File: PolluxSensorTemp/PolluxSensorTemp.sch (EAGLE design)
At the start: 0 parts

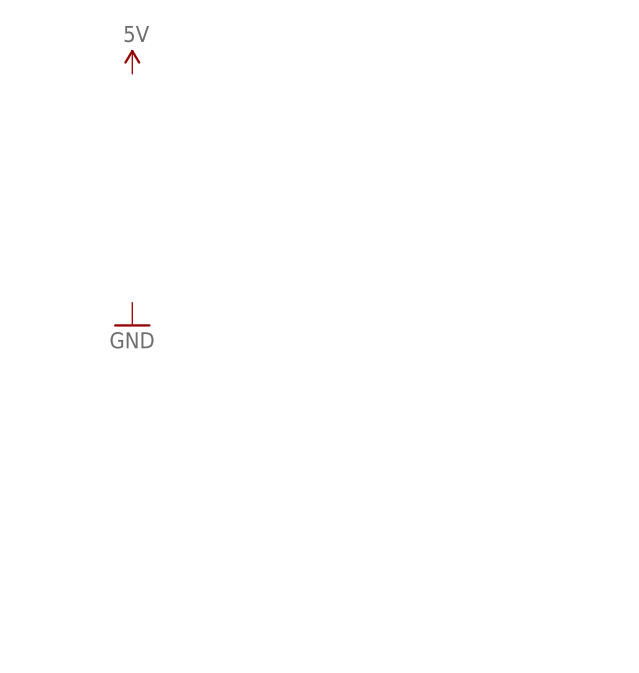
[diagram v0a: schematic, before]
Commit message: add Temp sensor board and schematics
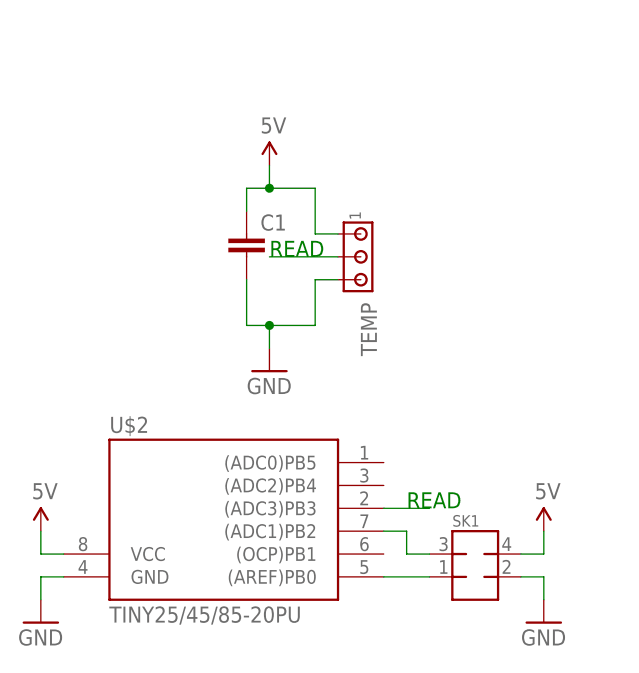
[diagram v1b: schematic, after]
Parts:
- added C1: (no value), SparkFun:CAPPTH1
- added SK1: (no value), jt-con-micromatch:MMATCH-8-PTH
- added TEMP: (no value), con-amp:MTA03-100
- added U$2: TINY25/45/85-20PU, avr-7:TINY25/45/85-20PU
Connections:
- new net 5V: C1.1, SK1.4, TEMP.1, U$2.VCC
- new net GND: C1.2, SK1.2, TEMP.3, U$2.GND
- new net N$1: SK1.3, U$2.(ADC1)PB2
- new net N$2: SK1.1, U$2.(AREF)PB0
- new net READ: TEMP.2, U$2.(ADC3)PB3
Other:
- note added: "READ"
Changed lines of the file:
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@@
 </classes>
 <parts>
+<part name="GND1" library="SparkFun" deviceset="GND" device=""/>
+<part name="SK1" library="jt-con-micromatch" deviceset="MMATCH-8-*" device="PTH"/>
+<part name="U$2" library="avr-7" deviceset="TINY25/45/85" device="-20PU"/>
+<part name="U$3" library="SparkFun" deviceset="5V" device=""/>
+<part name="U$4" library="SparkFun" deviceset="5V" device=""/>
+<part name="GND2" library="SparkFun" deviceset="GND" device=""/>
+<part name="TEMP" library="con-amp" deviceset="MTA03-100" device=""/>
+<part name="C1" library="SparkFun" deviceset="CAP" device="PTH1"/>
 <part name="U$1" library="SparkFun" deviceset="5V" device=""/>
-<part name="GND1" library="SparkFun" deviceset="GND" device=""/>
+<part name="GND3" library="SparkFun" deviceset="GND" device=""/>
 </parts>
 <sheets>
 <sheet>
 <plain>
+<text x="58.42" y="58.42" size="1.778" layer="91">READ</text>
+<text x="73.66" y="30.48" size="1.778" layer="91">READ</text>
 </plain>
 <instances>
-<instance part="U$1" gate="G$1" x="43.18" y="78.74"/>
-<instance part="GND1" gate="1" x="43.18" y="50.8"/>
+<instance part="GND1" gate="1" x="88.9" y="17.78"/>
+<instance part="SK1" gate="G$1" x="81.28" y="22.86"/>
+<instance part="U$2" gate="G$1" x="53.34" y="27.94"/>
+<instance part="U$3" gate="G$1" x="33.02" y="27.94"/>
+<instance part="U$4" gate="G$1" x="88.9" y="27.94"/>
+<instance part="GND2" gate="1" x="33.02" y="17.78"/>
+<instance part="TEMP" gate="G$1" x="68.58" y="58.42" rot="R270"/>
+<instance part="C1" gate="G$1" x="55.88" y="58.42"/>
+<instance part="U$1" gate="G$1" x="58.42" y="68.58"/>
+<instance part="GND3" gate="1" x="58.42" y="45.72"/>
 </instances>
 <busses>
 </busses>
 <nets>
+<net name="N$2" class="0">
+<segment>
+<pinref part="SK1" gate="G$1" pin="1"/>
+<pinref part="U$2" gate="G$1" pin="(AREF)PB0"/>
+<wire x1="76.2" y1="22.86" x2="71.12" y2="22.86" width="0.1524" layer="91"/>
+</segment>
+</net>
+<net name="5V" class="0">
+<segment>
+<pinref part="SK1" gate="G$1" pin="4"/>
+<wire x1="86.36" y1="25.4" x2="88.9" y2="25.4" width="0.1524" layer="91"/>
+<pinref part="U$4" gate="G$1" pin="5V"/>
+<wire x1="88.9" y1="25.4" x2="88.9" y2="27.94" width="0.1524" layer="91"/>
+</segment>
+<segment>
+<pinref part="U$2" gate="G$1" pin="VCC"/>
+<wire x1="35.56" y1="25.4" x2="33.02" y2="25.4" width="0.1524" layer="91"/>
+<pinref part="U$3" gate="G$1" pin="5V"/>
+<wire x1="33.02" y1="25.4" x2="33.02" y2="27.94" width="0.1524" layer="91"/>
+</segment>
+<segment>
+<pinref part="C1" gate="G$1" pin="1"/>
+<wire x1="55.88" y1="63.5" x2="55.88" y2="66.04" width="0.1524" layer="91"/>
+<wire x1="55.88" y1="66.04" x2="58.42" y2="66.04" width="0.1524" layer="91"/>
+<wire x1="58.42" y1="66.04" x2="63.5" y2="66.04" width="0.1524" layer="91"/>
+<wire x1="63.5" y1="66.04" x2="63.5" y2="60.96" width="0.1524" layer="91"/>
+<pinref part="TEMP" gate="G$1" pin="1"/>
+<wire x1="63.5" y1="60.96" x2="66.04" y2="60.96" width="0.1524" layer="91"/>
+<pinref part="U$1" gate="G$1" pin="5V"/>
+<wire x1="58.42" y1="68.58" x2="58.42" y2="66.04" width="0.1524" layer="91"/>
+<junction x="58.42" y="66.04"/>
+</segment>
+</net>
+<net name="GND" class="0">
+<segment>
+<pinref part="U$2" gate="G$1" pin="GND"/>
+<wire x1="35.56" y1="22.86" x2="33.02" y2="22.86" width="0.1524" layer="91"/>
+<pinref part="GND2" gate="1" pin="GND"/>
+<wire x1="33.02" y1="22.86" x2="33.02" y2="20.32" width="0.1524" layer="91"/>
+</segment>
+<segment>
+<pinref part="SK1" gate="G$1" pin="2"/>
+<wire x1="86.36" y1="22.86" x2="88.9" y2="22.86" width="0.1524" layer="91"/>
+<pinref part="GND1" gate="1" pin="GND"/>
+<wire x1="88.9" y1="22.86" x2="88.9" y2="20.32" width="0.1524" layer="91"/>
+</segment>
+<segment>
+<wire x1="58.42" y1="50.8" x2="63.5" y2="50.8" width="0.1524" layer="91"/>
+<wire x1="63.5" y1="50.8" x2="63.5" y2="55.88" width="0.1524" layer="91"/>
+<pinref part="TEMP" gate="G$1" pin="3"/>
+<wire x1="63.5" y1="55.88" x2="66.04" y2="55.88" width="0.1524" layer="91"/>
+<pinref part="GND3" gate="1" pin="GND"/>
+<wire x1="58.42" y1="48.26" x2="58.42" y2="50.8" width="0.1524" layer="91"/>
+<pinref part="C1" gate="G$1" pin="2"/>
+<wire x1="55.88" y1="55.88" x2="55.88" y2="50.8" width="0.1524" layer="91"/>
+<wire x1="55.88" y1="50.8" x2="58.42" y2="50.8" width="0.1524" layer="91"/>
+<junction x="58.42" y="50.8"/>
+</segment>
+</net>
+<net name="N$1" class="0">
+<segment>
+<pinref part="U$2" gate="G$1" pin="(ADC1)PB2"/>
+<wire x1="71.12" y1="27.94" x2="73.66" y2="27.94" width="0.1524" layer="91"/>
+<wire x1="73.66" y1="27.94" x2="73.66" y2="25.4" width="0.1524" layer="91"/>
+<pinref part="SK1" gate="G$1" pin="3"/>
+<wire x1="73.66" y1="25.4" x2="76.2" y2="25.4" width="0.1524" layer="91"/>
+</segment>
+</net>
+<net name="READ" class="0">
+<segment>
+<pinref part="U$2" gate="G$1" pin="(ADC3)PB3"/>
+<wire x1="71.12" y1="30.48" x2="76.2" y2="30.48" width="0.1524" layer="91"/>
+</segment>
+<segment>
+<pinref part="TEMP" gate="G$1" pin="2"/>
+<wire x1="66.04" y1="58.42" x2="58.42" y2="58.42" width="0.1524" layer="91"/>
+</segment>
+</net>
 </nets>
 </sheet>

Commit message: improve sensor board
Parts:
- removed SK1: (no value), jt-con-micromatch:MMATCH-8-PTH
- added C2: 1 uF, SparkFun:CAP_POLPTH2
- added SK2: (no value), jt-con-micromatch:MMATCH-8-PTH
- C1: value (none) -> 10 pF
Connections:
- removed net N$2: SK1.1, U$2.(AREF)PB0
- new net SDA: SK2.4, U$2.(AREF)PB0
- net 5V: now also C2.+, SK2.1; no longer SK1.4
- net GND: now also C2.-, SK2.2; no longer SK1.2
- net N$1: now also SK2.3; no longer SK1.3
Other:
- note added: "SCL"
- note added: "SDA"
- moved on the sheet: C1
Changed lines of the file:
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@@
 </classes>
 <parts>
-<part name="GND1" library="SparkFun" deviceset="GND" device=""/>
-<part name="SK1" library="jt-con-micromatch" deviceset="MMATCH-8-*" device="PTH"/>
 <part name="U$2" library="avr-7" deviceset="TINY25/45/85" device="-20PU"/>
 <part name="U$3" library="SparkFun" deviceset="5V" device=""/>
-<part name="U$4" library="SparkFun" deviceset="5V" device=""/>
 <part name="GND2" library="SparkFun" deviceset="GND" device=""/>
 <part name="TEMP" library="con-amp" deviceset="MTA03-100" device=""/>
-<part name="C1" library="SparkFun" deviceset="CAP" device="PTH1"/>
+<part name="C1" library="SparkFun" deviceset="CAP" device="PTH1" value="10 pF"/>
 <part name="U$1" library="SparkFun" deviceset="5V" device=""/>
 <part name="GND3" library="SparkFun" deviceset="GND" device=""/>
+<part name="SK2" library="jt-con-micromatch" deviceset="MMATCH-8-*" device="PTH"/>
+<part name="U$5" library="SparkFun" deviceset="5V" device=""/>
+<part name="GND4" library="SparkFun" deviceset="GND" device=""/>
+<part name="C2" library="SparkFun" deviceset="CAP_POL" device="PTH2" value="1 uF"/>
 </parts>
 <sheets>
@@
 <plain>
 <text x="58.42" y="58.42" size="1.778" layer="91">READ</text>
-<text x="73.66" y="30.48" size="1.778" layer="91">READ</text>
+<text x="71.12" y="30.48" size="1.778" layer="91">READ</text>
+<text x="71.12" y="27.94" size="1.778" layer="91">SCL</text>
+<text x="71.12" y="22.86" size="1.778" layer="91">SDA</text>
+<text x="91.44" y="27.94" size="1.778" layer="91">SDA</text>
 </plain>
 <instances>
-<instance part="GND1" gate="1" x="88.9" y="17.78"/>
-<instance part="SK1" gate="G$1" x="81.28" y="22.86"/>
 <instance part="U$2" gate="G$1" x="53.34" y="27.94"/>
 <instance part="U$3" gate="G$1" x="33.02" y="27.94"/>
-<instance part="U$4" gate="G$1" x="88.9" y="27.94"/>
 <instance part="GND2" gate="1" x="33.02" y="17.78"/>
 <instance part="TEMP" gate="G$1" x="68.58" y="58.42" rot="R270"/>
-<instance part="C1" gate="G$1" x="55.88" y="58.42"/>
+<instance part="C1" gate="G$1" x="53.34" y="58.42"/>
 <instance part="U$1" gate="G$1" x="58.42" y="68.58"/>
-<instance part="GND3" gate="1" x="58.42" y="45.72"/>
+<instance part="GND3" gate="1" x="58.42" y="48.26"/>
+<instance part="SK2" gate="G$1" x="86.36" y="25.4"/>
+<instance part="U$5" gate="G$1" x="78.74" y="35.56"/>
+<instance part="GND4" gate="1" x="93.98" y="17.78"/>
+<instance part="C2" gate="G$1" x="45.72" y="60.96"/>
 </instances>
 <busses>
 </busses>
 <nets>
-<net name="N$2" class="0">
-<segment>
-<pinref part="SK1" gate="G$1" pin="1"/>
-<pinref part="U$2" gate="G$1" pin="(AREF)PB0"/>
-<wire x1="76.2" y1="22.86" x2="71.12" y2="22.86" width="0.1524" layer="91"/>
-</segment>
-</net>
 <net name="5V" class="0">
-<segment>
-<pinref part="SK1" gate="G$1" pin="4"/>
-<wire x1="86.36" y1="25.4" x2="88.9" y2="25.4" width="0.1524" layer="91"/>
-<pinref part="U$4" gate="G$1" pin="5V"/>
-<wire x1="88.9" y1="25.4" x2="88.9" y2="27.94" width="0.1524" layer="91"/>
-</segment>
 <segment>
 <pinref part="U$2" gate="G$1" pin="VCC"/>
@@
 <segment>
 <pinref part="C1" gate="G$1" pin="1"/>
-<wire x1="55.88" y1="63.5" x2="55.88" y2="66.04" width="0.1524" layer="91"/>
-<wire x1="55.88" y1="66.04" x2="58.42" y2="66.04" width="0.1524" layer="91"/>
+<wire x1="53.34" y1="63.5" x2="53.34" y2="66.04" width="0.1524" layer="91"/>
+<wire x1="53.34" y1="66.04" x2="58.42" y2="66.04" width="0.1524" layer="91"/>
 <wire x1="58.42" y1="66.04" x2="63.5" y2="66.04" width="0.1524" layer="91"/>
 <wire x1="63.5" y1="66.04" x2="63.5" y2="60.96" width="0.1524" layer="91"/>
@@
 <wire x1="58.42" y1="68.58" x2="58.42" y2="66.04" width="0.1524" layer="91"/>
 <junction x="58.42" y="66.04"/>
+<pinref part="C2" gate="G$1" pin="+"/>
+<wire x1="45.72" y1="63.5" x2="45.72" y2="66.04" width="0.1524" layer="91"/>
+<wire x1="45.72" y1="66.04" x2="53.34" y2="66.04" width="0.1524" layer="91"/>
+<junction x="53.34" y="66.04"/>
+</segment>
+<segment>
+<pinref part="SK2" gate="G$1" pin="1"/>
+<pinref part="U$5" gate="G$1" pin="5V"/>
+<wire x1="81.28" y1="25.4" x2="78.74" y2="25.4" width="0.1524" layer="91"/>
+<wire x1="78.74" y1="25.4" x2="78.74" y2="35.56" width="0.1524" layer="91"/>
 </segment>
 </net>
@@
 </segment>
 <segment>
-<pinref part="SK1" gate="G$1" pin="2"/>
-<wire x1="86.36" y1="22.86" x2="88.9" y2="22.86" width="0.1524" layer="91"/>
-<pinref part="GND1" gate="1" pin="GND"/>
-<wire x1="88.9" y1="22.86" x2="88.9" y2="20.32" width="0.1524" layer="91"/>
-</segment>
-<segment>
-<wire x1="58.42" y1="50.8" x2="63.5" y2="50.8" width="0.1524" layer="91"/>
-<wire x1="63.5" y1="50.8" x2="63.5" y2="55.88" width="0.1524" layer="91"/>
+<wire x1="58.42" y1="53.34" x2="63.5" y2="53.34" width="0.1524" layer="91"/>
+<wire x1="63.5" y1="53.34" x2="63.5" y2="55.88" width="0.1524" layer="91"/>
 <pinref part="TEMP" gate="G$1" pin="3"/>
 <wire x1="63.5" y1="55.88" x2="66.04" y2="55.88" width="0.1524" layer="91"/>
 <pinref part="GND3" gate="1" pin="GND"/>
-<wire x1="58.42" y1="48.26" x2="58.42" y2="50.8" width="0.1524" layer="91"/>
+<wire x1="58.42" y1="50.8" x2="58.42" y2="53.34" width="0.1524" layer="91"/>
 <pinref part="C1" gate="G$1" pin="2"/>
-<wire x1="55.88" y1="55.88" x2="55.88" y2="50.8" width="0.1524" layer="91"/>
-<wire x1="55.88" y1="50.8" x2="58.42" y2="50.8" width="0.1524" layer="91"/>
-<junction x="58.42" y="50.8"/>
+<wire x1="53.34" y1="55.88" x2="53.34" y2="53.34" width="0.1524" layer="91"/>
+<wire x1="53.34" y1="53.34" x2="58.42" y2="53.34" width="0.1524" layer="91"/>
+<junction x="58.42" y="53.34"/>
+<pinref part="C2" gate="G$1" pin="-"/>
+<wire x1="53.34" y1="53.34" x2="45.72" y2="53.34" width="0.1524" layer="91"/>
+<wire x1="45.72" y1="53.34" x2="45.72" y2="55.88" width="0.1524" layer="91"/>
+<junction x="53.34" y="53.34"/>
+</segment>
+<segment>
+<pinref part="SK2" gate="G$1" pin="2"/>
+<pinref part="GND4" gate="1" pin="GND"/>
+<wire x1="91.44" y1="25.4" x2="93.98" y2="25.4" width="0.1524" layer="91"/>
+<wire x1="93.98" y1="25.4" x2="93.98" y2="20.32" width="0.1524" layer="91"/>
 </segment>
 </net>
@@
 <segment>
 <pinref part="U$2" gate="G$1" pin="(ADC1)PB2"/>
-<wire x1="71.12" y1="27.94" x2="73.66" y2="27.94" width="0.1524" layer="91"/>
-<wire x1="73.66" y1="27.94" x2="73.66" y2="25.4" width="0.1524" layer="91"/>
-<pinref part="SK1" gate="G$1" pin="3"/>
-<wire x1="73.66" y1="25.4" x2="76.2" y2="25.4" width="0.1524" layer="91"/>
+<pinref part="SK2" gate="G$1" pin="3"/>
+<wire x1="71.12" y1="27.94" x2="81.28" y2="27.94" width="0.1524" layer="91"/>
 </segment>
 </net>
@@
 <segment>
 <pinref part="U$2" gate="G$1" pin="(ADC3)PB3"/>
-<wire x1="71.12" y1="30.48" x2="76.2" y2="30.48" width="0.1524" layer="91"/>
+<wire x1="71.12" y1="30.48" x2="73.66" y2="30.48" width="0.1524" layer="91"/>
 </segment>
 <segment>
@@
 </segment>
 </net>
+<net name="SDA" class="0">
+<segment>
+<pinref part="U$2" gate="G$1" pin="(AREF)PB0"/>
+<wire x1="76.2" y1="22.86" x2="71.12" y2="22.86" width="0.1524" layer="91"/>
+</segment>
+<segment>
+<pinref part="SK2" gate="G$1" pin="4"/>
+<wire x1="91.44" y1="27.94" x2="96.52" y2="27.94" width="0.1524" layer="91"/>
+</segment>
+</net>
